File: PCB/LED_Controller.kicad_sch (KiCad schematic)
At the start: 40 parts, among them J1 Barrel_Jack, J2 Conn_01x06_Female, J4 Add. LED Strip, J7 Conn_01x02, U1 ESP32-PICO-D4, U2 AP62200, U4 74LVCH2T45DC, U5 LAN8720A, U6 MCP1792x-5002xCB, Y1 Crystal_GND23

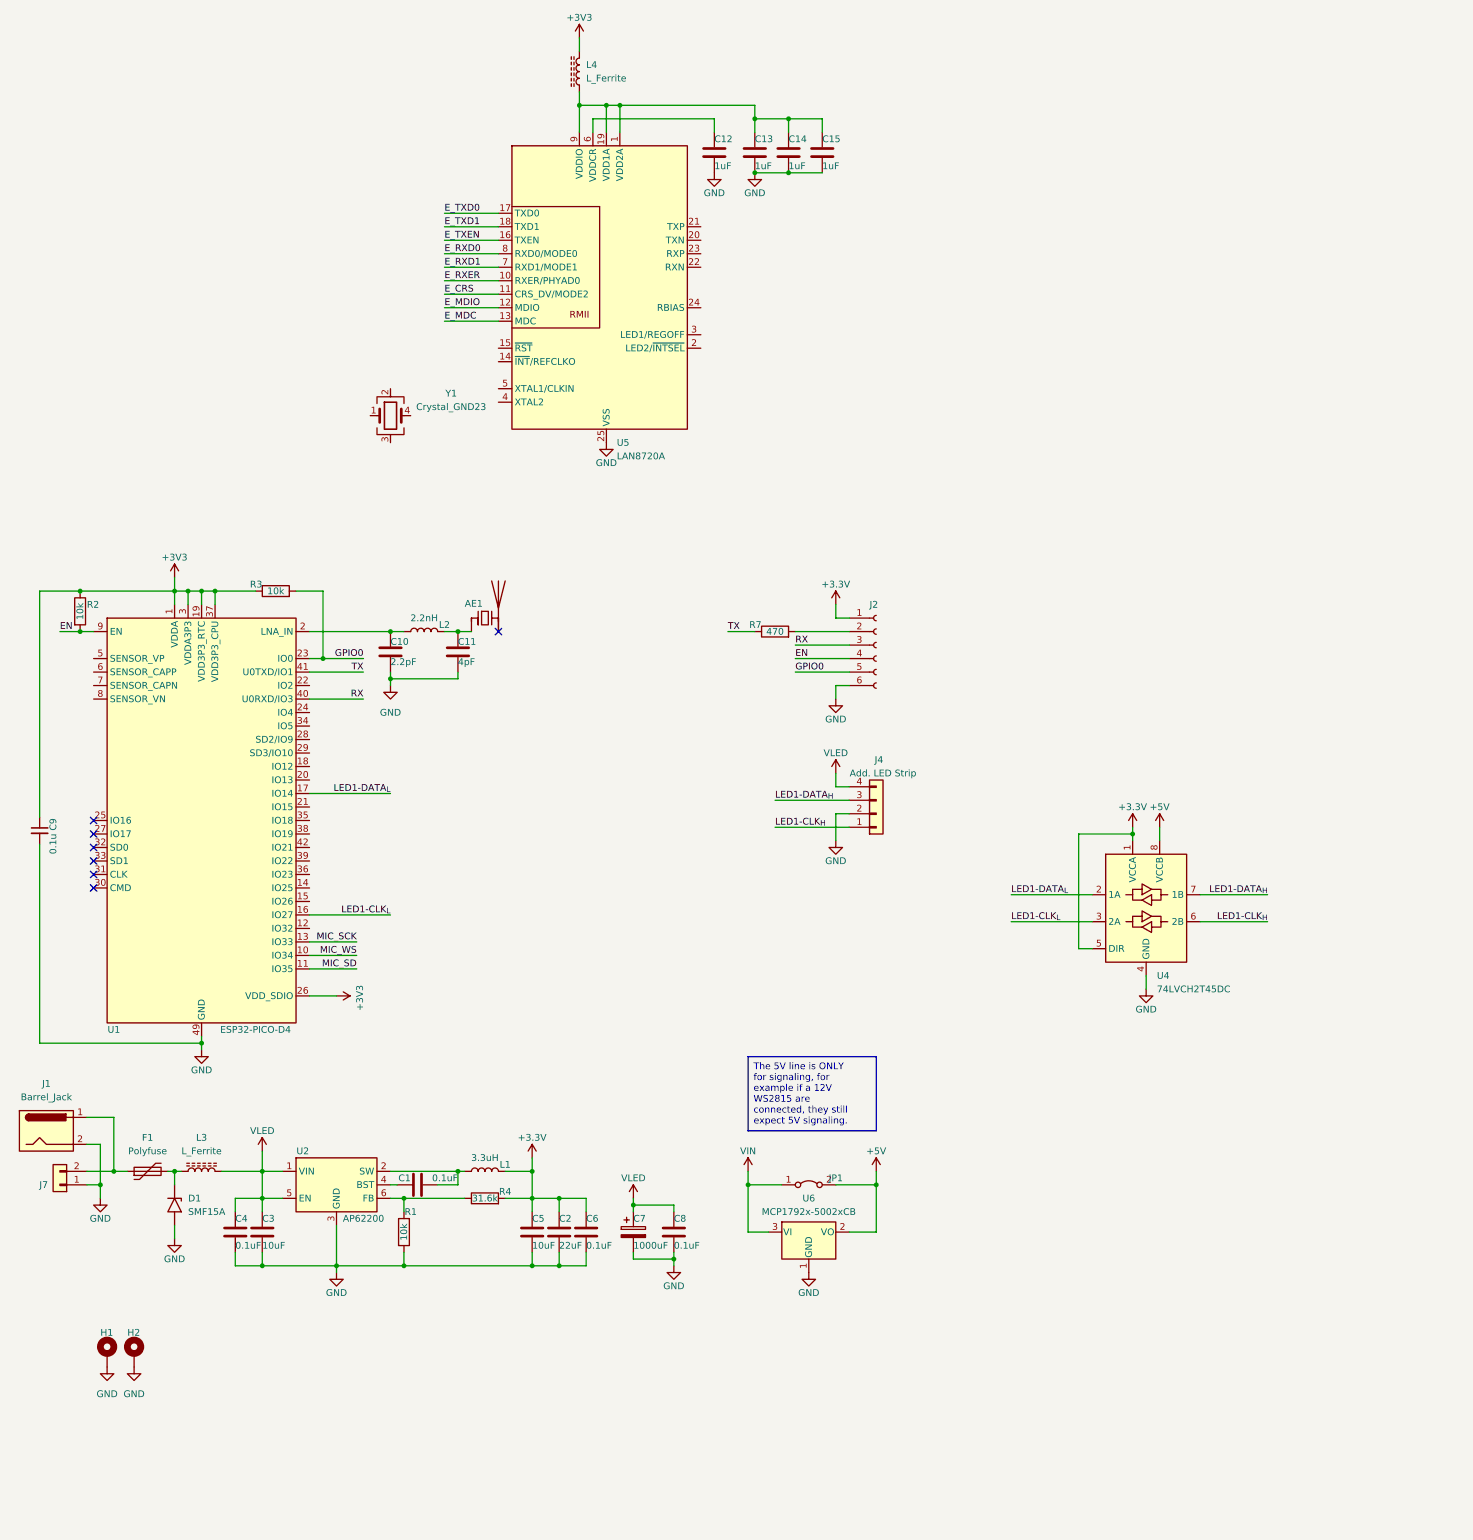
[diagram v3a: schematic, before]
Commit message: More work, added ethernet controller and ethernet pin
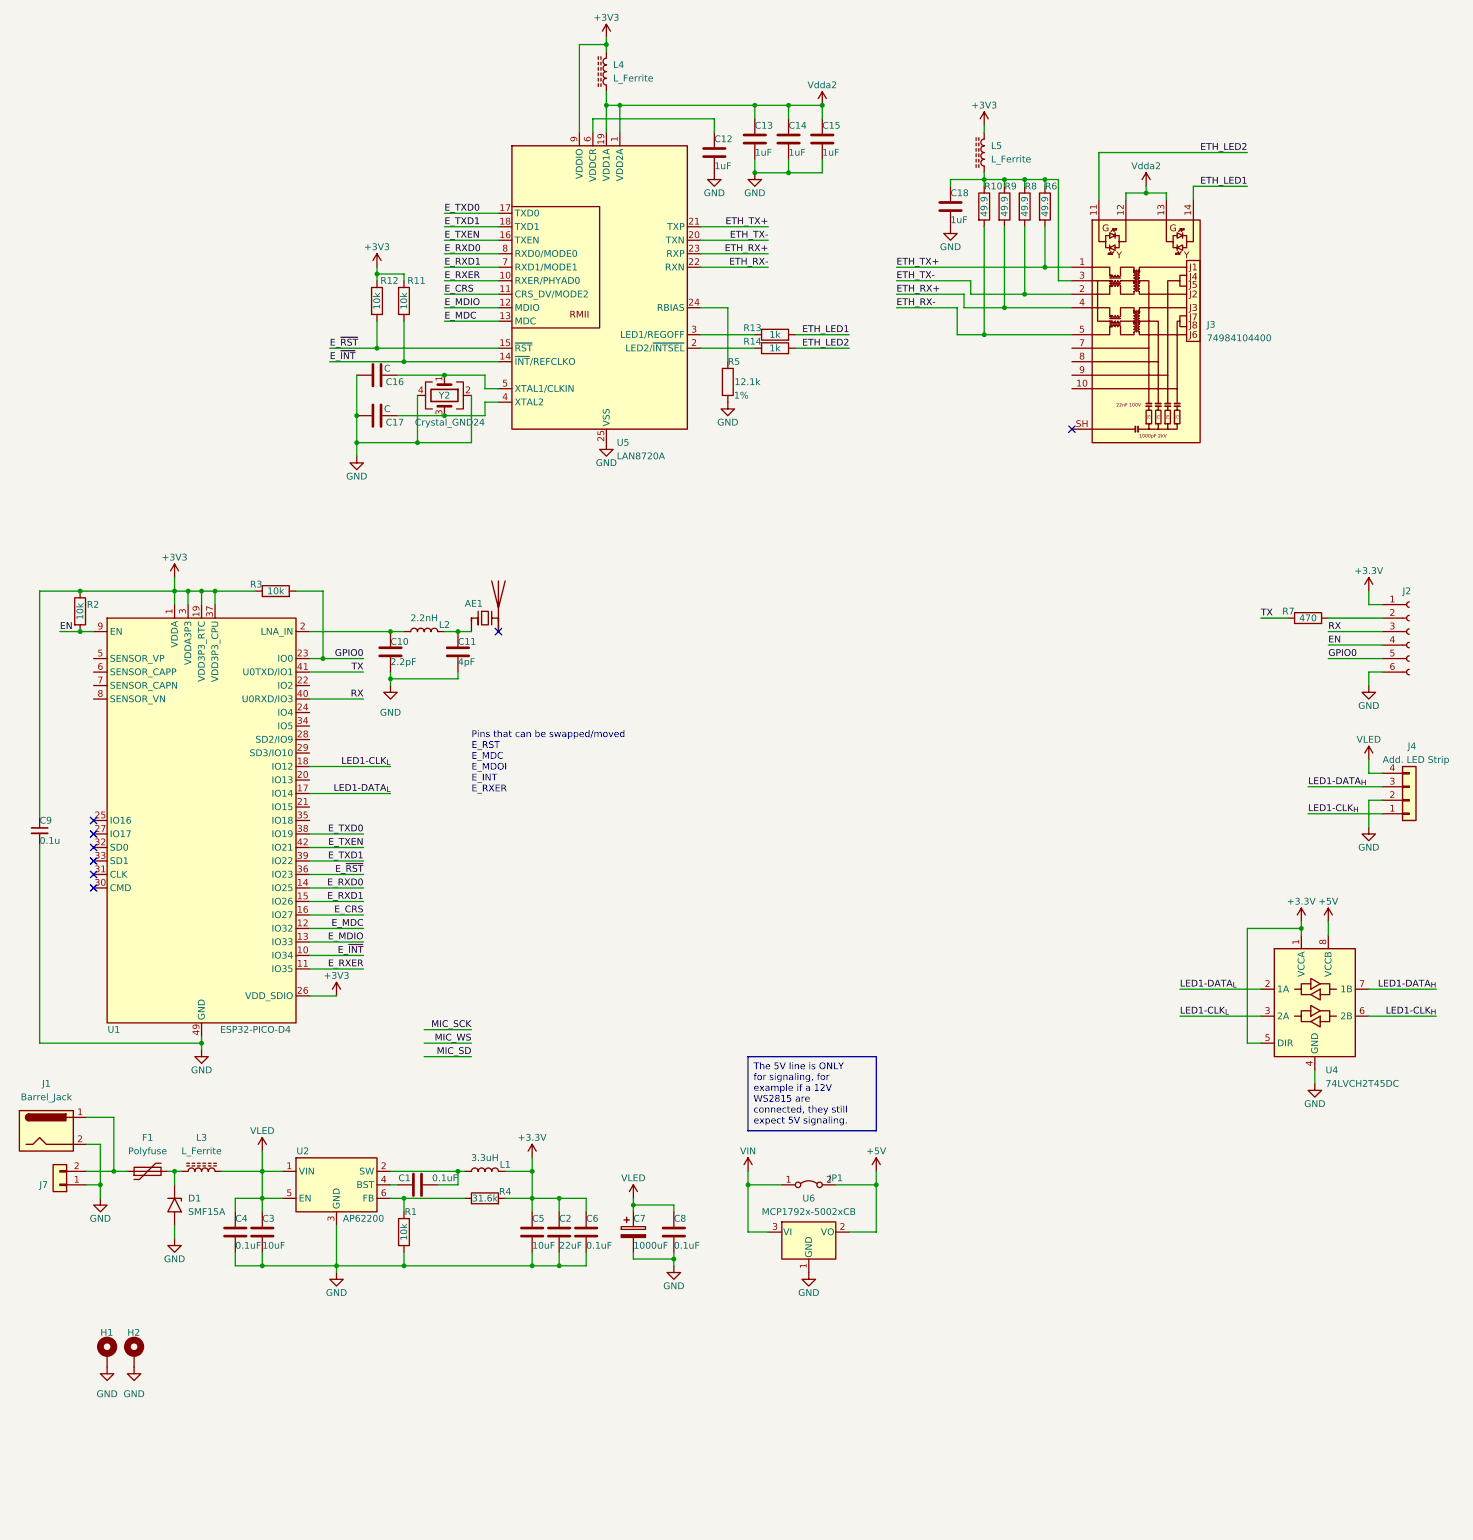
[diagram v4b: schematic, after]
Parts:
- removed Y1: Crystal_GND23, symbol Device:Crystal_GND23
- added C16, C17: C, symbol Device:C
- added C18: 1uF, symbol Device:C
- added J3: 74984104400, Connector_RJ:RJ45_UDE_RB1-125B8G1A, symbol Connector:74984104400
- added L5: L_Ferrite, symbol Device:L_Ferrite
- added R10, R6, R8, R9: 49.9, symbol Device:R
- added R11, R12: 10k, symbol Device:R
- added R13, R14: 1k, symbol Device:R
- added R5: 12.1k, symbol Device:R
- added Y2: Crystal_GND24, symbol Device:Crystal_GND24
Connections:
- net +3V3: now also U5.9 (VDDIO), L5.2, R11.1, R12.1
- net E_CRS: now also U1.16 (IO27)
- net E_MDC: now also U1.12 (IO32)
- net E_MDIO: now also U1.13 (IO33)
- net E_RXD0: now also U1.14 (IO25)
- net E_RXD1: now also U1.15 (IO26)
- net E_RXER: now also U1.11 (IO35)
- net E_TXD0: now also U1.38 (IO19)
- net E_TXD1: now also U1.39 (IO22)
- net E_TXEN: now also U1.42 (IO21)
- net GND: now also C16.1, C17.1, C18.2, R5.2, Y2.2, Y2.4
- net LED1-CLK_{L}: now also U1.18 (IO12); no longer U1.16 (IO27)
- net MIC_SCK: no longer U1.13 (IO33)
- net MIC_SD: no longer U1.11 (IO35)
- net MIC_WS: no longer U1.10 (IO34)
- net Vdda2: now reaches C13.1, C14.1, C15.1, L4.1, U5.1 (VDD2A), U5.19 (VDD1A)
- net Vdda2: now also J3.12, J3.13; no longer U5.9 (VDDIO)
- net E_~{INT}: now reaches U5.14 (~{INT}/REFCLKO)
- net E_~{INT}: now also U1.10 (IO34), R11.2
- net E_~{RST}: now reaches U5.15 (~{RST})
- net E_~{RST}: now also U1.36 (IO23), R12.2
- net at U5.2 (LED2/~{INTSEL}): now also R14.1
- net ETH_TX-: now reaches U5.20 (TXN)
- net ETH_TX-: now also J3.2 (TD-), R8.2
- net ETH_TX+: now reaches U5.21 (TXP)
- net ETH_TX+: now also J3.1 (TD+), R6.2
- net ETH_RX-: now reaches U5.22 (RXN)
- net ETH_RX-: now also J3.5 (RD-), R10.2
- net ETH_RX+: now reaches U5.23 (RXP)
- net ETH_RX+: now also J3.4 (RD+), R9.2
- net at U5.24 (RBIAS): now also R5.1
- net at U5.3 (LED1/REGOFF): now also R13.1
- net at U5.4 (XTAL2): now also C17.2, Y2.3
- net at U5.5 (XTAL1/CLKIN): now also C16.2, Y2.1
- new net: C18.1, J3.3 (CD), L5.1, R10.1, R6.1, R8.1, R9.1
- new net ETH_LED1: J3.14, R13.2
- new net ETH_LED2: J3.11, R14.2
- no-connect marks 7 -> 8
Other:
- note added: "Pins that can be swapped/moved E_RST E_MDC E_MDOI E_INT E_RXER"
- moved on the sheet: C13, C14, C15, J2, J4, L4, R7, U4

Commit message: Moved new symbol to internal library
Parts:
- removed J3: 74984104400, Connector_RJ:RJ45_UDE_RB1-125B8G1A, symbol Connector:74984104400
- added J3: 74984104400, Connector_RJ:RJ45_UDE_RB1-125B8G1A, symbol ProjectLibrary:74984104400
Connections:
- net ETH_LED1: now also J3.14
- net ETH_LED2: now also J3.11
- net ETH_RX+: now also J3.4 (RD+)
- net ETH_RX-: now also J3.5 (RD-)
- net ETH_TX+: now also J3.1 (TD+)
- net ETH_TX-: now also J3.2 (TD-)
- net Vdda2: now also J3.12, J3.13
- net at C18.1, L5.1, R10.1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: now also J3.3 (CD)

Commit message: More work, including hierarchical sheets breakout
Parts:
- removed C1, C4, C6, C8: 0.1uF, Capacitor_SMD:C_0805_2012Metric_Pad1.18x1.45mm_HandSolder, symbol Device:C
- removed C12, C13, C14, C15, C18: 1uF, symbol Device:C
- removed C16, C17: C, symbol Device:C
- removed C2: 22uF, Capacitor_SMD:C_1206_3216Metric_Pad1.33x1.80mm_HandSolder, symbol Device:C
- removed C3: 10uF, Capacitor_SMD:C_0805_2012Metric_Pad1.18x1.45mm_HandSolder, symbol Device:C
- removed C5: 10uF, Capacitor_SMD:C_1206_3216Metric_Pad1.33x1.80mm_HandSolder, symbol Device:C
- removed C7: 1000uF, Capacitor_THT:CP_Radial_D10.0mm_P5.00mm_P7.50mm, symbol Device:C_Polarized
- removed D1: SMF15A, Diode_SMD:D_SMF, symbol Diode:SMF15A
- removed F1: Polyfuse, symbol Device:Polyfuse
- removed J1: Barrel_Jack, Connector_BarrelJack:BarrelJack_Horizontal, symbol Connector:Barrel_Jack
- removed J3: 74984104400, Connector_RJ:RJ45_UDE_RB1-125B8G1A, symbol ProjectLibrary:74984104400
- removed J4: Add. LED Strip, TerminalBlock_Phoenix:TerminalBlock_Phoenix_MKDS-1,5-4-5.08_1x04_P5.08mm_Horizontal, symbol Connector_Generic:Conn_01x04
- removed J7: Conn_01x02, TerminalBlock_Phoenix:TerminalBlock_Phoenix_MKDS-1,5-2-5.08_1x02_P5.08mm_Horizontal, symbol Connector_Generic:Conn_01x02
- removed JP1: Jumper_2_Bridged, Jumper:SolderJumper-2_P1.3mm_Bridged2Bar_Pad1.0x1.5mm, symbol Jumper:Jumper_2_Bridged
- removed L1: 3.3uH, Inductor_SMD:L_1206_3216Metric_Pad1.22x1.90mm_HandSolder, symbol Device:L
- removed L3, L4, L5: L_Ferrite, symbol Device:L_Ferrite
- removed R1: 10k, Resistor_SMD:R_0805_2012Metric_Pad1.20x1.40mm_HandSolder, symbol Device:R
- removed R10, R6, R8, R9: 49.9, symbol Device:R
- removed R11, R12: 10k, symbol Device:R
- removed R13, R14: 1k, symbol Device:R
- removed R4: 31.6k, Resistor_SMD:R_0805_2012Metric_Pad1.20x1.40mm_HandSolder, symbol Device:R
- removed R5: 12.1k, symbol Device:R
- removed U2: AP62200, Package_TO_SOT_SMD:SOT-563, symbol Regulator_Switching:AP62250Z6
- removed U5: LAN8720A, Package_DFN_QFN:VQFN-24-1EP_4x4mm_P0.5mm_EP2.5x2.5mm_ThermalVias, symbol Interface_Ethernet:LAN8720A
- removed U6: MCP1792x-5002xCB, Package_TO_SOT_SMD:SOT-23, symbol Regulator_Linear:MCP1792x-5002xCB
- removed Y2: Crystal_GND24, symbol Device:Crystal_GND24
- added J5: Screw_Terminal_01x04, TerminalBlock_Phoenix:TerminalBlock_Phoenix_MKDS-1,5-4-5.08_1x04_P5.08mm_Horizontal, symbol Connector:Screw_Terminal_01x04
- added R23, R27, R28: 10k, Resistor_SMD:R_0805_2012Metric_Pad1.20x1.40mm_HandSolder, symbol Device:R
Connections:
- net +3V3: now also R23.2, R27.2, R28.2
- net GND: now also J5.3 (Pin_3)
- net LED1-CLK_{H}: now also J5.4 (Pin_4)
- net LED1-DATA_{H}: now also J5.2 (Pin_2)
- net VLED: now also J5.1 (Pin_1)
- net POE_TPH: now reaches U1.28 (SD2/IO9)
- net POE_TPH: now also R27.1
- net POE_~{BT}: now reaches U1.29 (SD3/IO10)
- net POE_~{BT}: now also R23.1
- net POE_TPL: now reaches U1.34 (IO5)
- net POE_TPL: now also R28.1
- no-connect marks 8 -> 7
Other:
- added sheet Ethernet and Connector (ethernet.kicad_sch)
- added sheet POE and External Power (poe_power.kicad_sch)
- note added: "Pins that can be swapped/moved E_RST E_MDC E_MDOI E_INT E_RXER LED1-CLK_{L} LED1-DATA_{L} POE_~{BT} POE_TPH POE_TPL"
- note removed: "Pins that can be swapped/moved E_RST E_MDC E_MDOI E_INT E_RXER"
- moved on the sheet: AE1, C10, C11, C9, H1, H2, J2, L2, R2, R3, R7, U1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

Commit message: Started on board layout
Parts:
- C10, C11: footprint Capacitor_SMD:C_0805_2012Metric_Pad1.18x1.45mm_HandSolder -> Capacitor_SMD:C_0805_2012Metric
- C9: footprint Capacitor_SMD:C_0603_1608Metric -> Capacitor_SMD:C_0805_2012Metric
- R23, R27, R28, R7: footprint Resistor_SMD:R_0805_2012Metric_Pad1.20x1.40mm_HandSolder -> Resistor_SMD:R_0805_2012Metric
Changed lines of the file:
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@@
       (effects (font (size 1.27 1.27)) (justify left))
     )
-    (property "Footprint" "Capacitor_SMD:C_0603_1608Metric" (at 30.48 140.335 0)
+    (property "Footprint" "Capacitor_SMD:C_0805_2012Metric" (at 30.48 140.335 0)
       (effects (font (size 1.27 1.27)) hide)
     )
@@
       (effects (font (size 1.27 1.27)))
     )
-    (property "Footprint" "Resistor_SMD:R_0805_2012Metric_Pad1.20x1.40mm_HandSolder" (at 183.642 152.4 90)
+    (property "Footprint" "Resistor_SMD:R_0805_2012Metric" (at 183.642 152.4 90)
       (effects (font (size 1.27 1.27)) hide)
     )
@@
       (effects (font (size 1.27 1.27)))
     )
-    (property "Footprint" "Resistor_SMD:R_0805_2012Metric_Pad1.20x1.40mm_HandSolder" (at 181.102 152.4 90)
+    (property "Footprint" "Resistor_SMD:R_0805_2012Metric" (at 181.102 152.4 90)
       (effects (font (size 1.27 1.27)) hide)
     )
@@
       (effects (font (size 1.27 1.27)))
     )
-    (property "Footprint" "Resistor_SMD:R_0805_2012Metric_Pad1.20x1.40mm_HandSolder" (at 227.33 70.358 90)
+    (property "Footprint" "Resistor_SMD:R_0805_2012Metric" (at 227.33 70.358 90)
       (effects (font (size 1.27 1.27)) hide)
     )
@@
       (effects (font (size 1.27 1.27)) (justify left))
     )
-    (property "Footprint" "Capacitor_SMD:C_0805_2012Metric_Pad1.18x1.45mm_HandSolder" (at 97.4852 110.49 0)
+    (property "Footprint" "Capacitor_SMD:C_0805_2012Metric" (at 97.4852 110.49 0)
       (effects (font (size 1.27 1.27)) hide)
     )
@@
       (effects (font (size 1.27 1.27)))
     )
-    (property "Footprint" "Resistor_SMD:R_0805_2012Metric_Pad1.20x1.40mm_HandSolder" (at 178.562 152.4 90)
+    (property "Footprint" "Resistor_SMD:R_0805_2012Metric" (at 178.562 152.4 90)
       (effects (font (size 1.27 1.27)) hide)
     )
@@
       (effects (font (size 1.27 1.27)) (justify left))
     )
-    (property "Footprint" "Capacitor_SMD:C_0805_2012Metric_Pad1.18x1.45mm_HandSolder" (at 110.1852 110.49 0)
-      (effects (font (size 1.27 1.27)) hide)
-    )
+    (property "Footprint" "Capacitor_SMD:C_0805_2012Metric" (at 110.1852 110.49 0)
+      (effects (font (size 1.27 1.27)) hide)
+    )

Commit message: Started serious board layout
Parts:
- added C26, C27: 0.1u, Capacitor_SMD:C_0805_2012Metric, symbol Device:C_Small
- added H3: MountingHole_Pad, MountingHole:MountingHole_3.2mm_M3_DIN965_Pad, symbol Mechanical:MountingHole_Pad
- J2: footprint Connector_PinHeader_2.54mm:PinHeader_1x06_P2.54mm_Horizontal -> Connector:Tag-Connect_TC2030-IDC-NL_2x03_P1.27mm_Vertical
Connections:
- net +3V3: now also C26.1, C27.1
- net GND: now also C26.2, C27.2, H3.1
- net LED1-CLK_{H}: now also U4.7 (1B); no longer U4.6 (2B)
- net LED1-CLK_{L}: now also U4.2 (1A); no longer U4.3 (2A)
- net LED1-DATA_{H}: now also U4.6 (2B); no longer U4.7 (1B)
- net LED1-DATA_{L}: now also U4.3 (2A); no longer U4.2 (1A)
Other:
- sheet POE and External Power ports: added POE_DIS; removed none
- moved on the sheet: C9
